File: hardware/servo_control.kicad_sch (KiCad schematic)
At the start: 4 parts, among them J5 Conn_01x03, J6 Conn_01x03, J7 Conn_01x03, J8 Conn_01x03

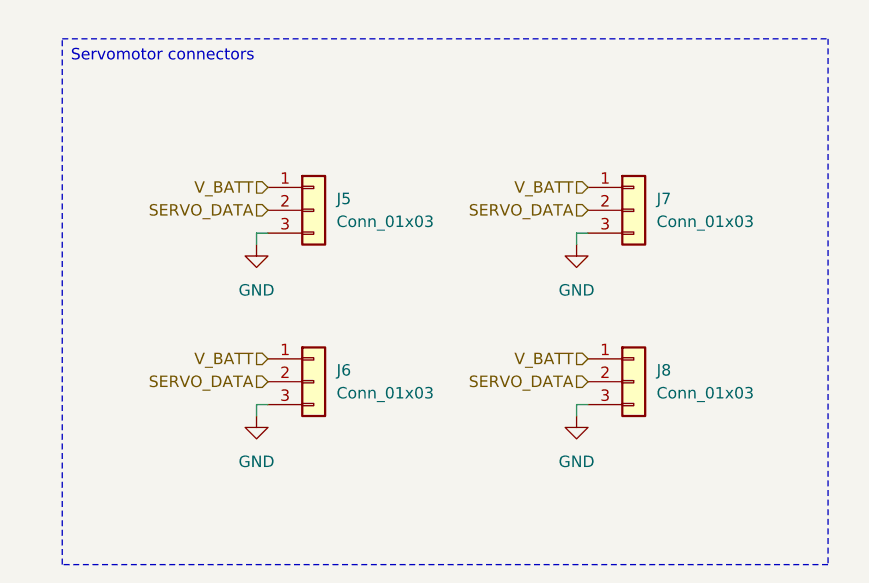
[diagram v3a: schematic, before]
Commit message: Adding test points
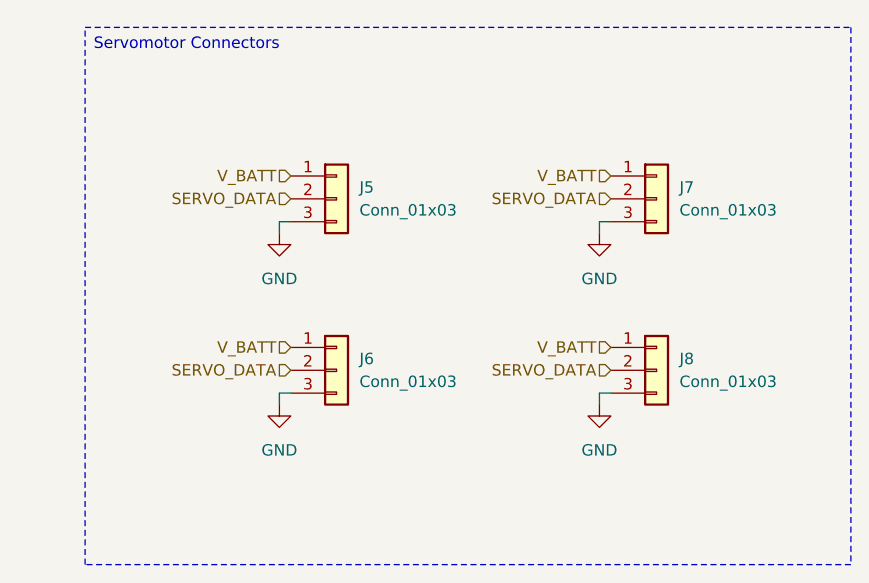
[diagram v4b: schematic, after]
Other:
- moved on the sheet: J5, J6, J7, J8
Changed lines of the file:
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@@
 		(comment 1 "Ousmane THIONGANE")
 	)
-	(text_box "Servomotor connectors"
+	(text_box "Servomotor Connectors"
 		(exclude_from_sim no)
-		(at 104.14 72.39 0)
-		(size 85.09 58.42)
+		(at 106.68 71.12 0)
+		(size 85.09 59.69)
 		(margins 0.9525 0.9525 0.9525 0.9525)
 		(stroke
@@
 	(wire
 		(pts
-			(xy 161.29 113.03) (xy 161.29 114.3)
+			(xy 163.83 111.76) (xy 163.83 113.03)
 		)
 		(stroke
@@
 	(wire
 		(pts
-			(xy 162.56 93.98) (xy 161.29 93.98)
+			(xy 165.1 92.71) (xy 163.83 92.71)
 		)
 		(stroke
@@
 	(wire
 		(pts
-			(xy 125.73 93.98) (xy 125.73 95.25)
+			(xy 128.27 92.71) (xy 128.27 93.98)
 		)
 		(stroke
@@
 	(wire
 		(pts
-			(xy 127 113.03) (xy 125.73 113.03)
+			(xy 129.54 111.76) (xy 128.27 111.76)
 		)
 		(stroke
@@
 	(wire
 		(pts
-			(xy 162.56 113.03) (xy 161.29 113.03)
+			(xy 165.1 111.76) (xy 163.83 111.76)
 		)
 		(stroke
@@
 	(wire
 		(pts
-			(xy 127 93.98) (xy 125.73 93.98)
+			(xy 129.54 92.71) (xy 128.27 92.71)
 		)
 		(stroke
@@
 	(wire
 		(pts
-			(xy 125.73 113.03) (xy 125.73 114.3)
+			(xy 128.27 111.76) (xy 128.27 113.03)
 		)
 		(stroke
@@
 	(wire
 		(pts
-			(xy 161.29 93.98) (xy 161.29 95.25)
+			(xy 163.83 92.71) (xy 163.83 93.98)
 		)
 		(stroke
@@
 	(hierarchical_label "SERVO_DATA"
 		(shape input)
-		(at 127 110.49 180)
+		(at 129.54 109.22 180)
 		(effects
 			(font
@@
 	(hierarchical_label "SERVO_DATA"
 		(shape input)
-		(at 162.56 91.44 180)
+		(at 165.1 90.17 180)
 		(effects
 			(font
@@
 	(hierarchical_label "SERVO_DATA"
 		(shape input)
-		(at 127 91.44 180)
+		(at 129.54 90.17 180)
 		(effects
 			(font
@@
 	(hierarchical_label "V_BATT"
 		(shape input)
-		(at 162.56 88.9 180)
+		(at 165.1 87.63 180)
 		(effects
 			(font
@@
 	(hierarchical_label "SERVO_DATA"
 		(shape input)
-		(at 162.56 110.49 180)
+		(at 165.1 109.22 180)
 		(effects
 			(font
@@
 	(hierarchical_label "V_BATT"
 		(shape input)
-		(at 127 107.95 180)
+		(at 129.54 106.68 180)
 		(effects
 			(font
@@
 	(hierarchical_label "V_BATT"
 		(shape input)
-		(at 127 88.9 180)
+		(at 129.54 87.63 180)
 		(effects
 			(font
@@
 	(hierarchical_label "V_BATT"
 		(shape input)
-		(at 162.56 107.95 180)
+		(at 165.1 106.68 180)
 		(effects
 			(font
@@
 	(symbol
 		(lib_id "power:GND")
-		(at 161.29 95.25 0)
+		(at 163.83 93.98 0)
 		(unit 1)
 		(exclude_from_sim no)
@@
 		(fields_autoplaced yes)
 		(property "Reference" "#PWR056"
-			(at 161.29 101.6 0)
+			(at 163.83 100.33 0)
 			(effects
 				(font
@@
 		)
 		(property "Value" "GND"
-			(at 161.29 100.33 0)
+			(at 163.83 99.06 0)
 			(effects
 				(font
@@
 		)
 		(property "Footprint" ""
-			(at 161.29 95.25 0)
+			(at 163.83 93.98 0)
 			(effects
 				(font
@@
 		)
 		(property "Datasheet" ""
-			(at 161.29 95.25 0)
+			(at 163.83 93.98 0)
 			(effects
 				(font
@@
 		)
 		(property "Description" "Power symbol creates a global label with name \"GND\" , ground"
-			(at 161.29 95.25 0)
+			(at 163.83 93.98 0)
 			(effects
 				(font
@@
 	(symbol
 		(lib_id "power:GND")
-		(at 125.73 95.25 0)
+		(at 128.27 93.98 0)
 		(unit 1)
 		(exclude_from_sim no)
@@
 		(fields_autoplaced yes)
 		(property "Reference" "#PWR054"
-			(at 125.73 101.6 0)
+			(at 128.27 100.33 0)
 			(effects
 				(font
@@
 		)
 		(property "Value" "GND"
-			(at 125.73 100.33 0)
+			(at 128.27 99.06 0)
 			(effects
 				(font
@@
 		)
 		(property "Footprint" ""
-			(at 125.73 95.25 0)
+			(at 128.27 93.98 0)
 			(effects
 				(font
@@
 		)
 		(property "Datasheet" ""
-			(at 125.73 95.25 0)
+			(at 128.27 93.98 0)
 			(effects
 				(font
@@
 		)
 		(property "Description" "Power symbol creates a global label with name \"GND\" , ground"
-			(at 125.73 95.25 0)
+			(at 128.27 93.98 0)
 			(effects
 				(font
@@
 	(symbol
 		(lib_id "Connector_Generic:Conn_01x03")
-		(at 132.08 110.49 0)
+		(at 134.62 109.22 0)
 		(unit 1)
 		(exclude_from_sim no)
@@
 		(fields_autoplaced yes)
 		(property "Reference" "J6"
-			(at 134.62 109.2199 0)
+			(at 137.16 107.9499 0)
 			(effects
 				(font
@@
 		)
 		(property "Value" "Conn_01x03"
-			(at 134.62 111.7599 0)
+			(at 137.16 110.4899 0)
 			(effects
 				(font
@@
 		)
 		(property "Footprint" ""
-			(at 132.08 110.49 0)
+			(at 134.62 109.22 0)
 			(effects
 				(font
@@
 		)
 		(property "Datasheet" "~"
-			(at 132.08 110.49 0)
+			(at 134.62 109.22 0)
 			(effects
 				(font
@@
 		)
 		(property "Description" "Generic connector, single row, 01x03, script generated (kicad-library-utils/schlib/autogen/connector/)"
-			(at 132.08 110.49 0)
+			(at 134.62 109.22 0)
 			(effects
 				(font
@@
 	(symbol
 		(lib_id "power:GND")
-		(at 161.29 114.3 0)
+		(at 163.83 113.03 0)
 		(unit 1)
 		(exclude_from_sim no)
@@
 		(fields_autoplaced yes)
 		(property "Reference" "#PWR057"
-			(at 161.29 120.65 0)
+			(at 163.83 119.38 0)
 			(effects
 				(font
@@
 		)
 		(property "Value" "GND"
-			(at 161.29 119.38 0)
+			(at 163.83 118.11 0)
 			(effects
 				(font
@@
 		)
 		(property "Footprint" ""
-			(at 161.29 114.3 0)
+			(at 163.83 113.03 0)
 			(effects
 				(font
@@
 		)
 		(property "Datasheet" ""
-			(at 161.29 114.3 0)
+			(at 163.83 113.03 0)
 			(effects
 				(font
@@
 		)
 		(property "Description" "Power symbol creates a global label with name \"GND\" , ground"
-			(at 161.29 114.3 0)
+			(at 163.83 113.03 0)
 			(effects
 				(font
@@
 	(symbol
 		(lib_id "Connector_Generic:Conn_01x03")
-		(at 167.64 110.49 0)
+		(at 170.18 109.22 0)
 		(unit 1)
 		(exclude_from_sim no)
@@
 		(fields_autoplaced yes)
 		(property "Reference" "J8"
-			(at 170.18 109.2199 0)
+			(at 172.72 107.9499 0)
 			(effects
 				(font
@@
 		)
 		(property "Value" "Conn_01x03"
-			(at 170.18 111.7599 0)
+			(at 172.72 110.4899 0)
 			(effects
 				(font
@@
 		)
 		(property "Footprint" ""
-			(at 167.64 110.49 0)
+			(at 170.18 109.22 0)
 			(effects
 				(font
@@
 		)
 		(property "Datasheet" "~"
-			(at 167.64 110.49 0)
+			(at 170.18 109.22 0)
 			(effects
 				(font
@@
 		)
 		(property "Description" "Generic connector, single row, 01x03, script generated (kicad-library-utils/schlib/autogen/connector/)"
-			(at 167.64 110.49 0)
+			(at 170.18 109.22 0)
 			(effects
 				(font
@@
 	(symbol
 		(lib_id "power:GND")
-		(at 125.73 114.3 0)
+		(at 128.27 113.03 0)
 		(unit 1)
 		(exclude_from_sim no)
@@
 		(fields_autoplaced yes)
 		(property "Reference" "#PWR055"
-			(at 125.73 120.65 0)
+			(at 128.27 119.38 0)
 			(effects
 				(font
@@
 		)
 		(property "Value" "GND"
-			(at 125.73 119.38 0)
+			(at 128.27 118.11 0)
 			(effects
 				(font
@@
 		)
 		(property "Footprint" ""
-			(at 125.73 114.3 0)
+			(at 128.27 113.03 0)
 			(effects
 				(font
@@
 		)
 		(property "Datasheet" ""
-			(at 125.73 114.3 0)
+			(at 128.27 113.03 0)
 			(effects
 				(font
@@
 		)
 		(property "Description" "Power symbol creates a global label with name \"GND\" , ground"
-			(at 125.73 114.3 0)
+			(at 128.27 113.03 0)
 			(effects
 				(font
@@
 	(symbol
 		(lib_id "Connector_Generic:Conn_01x03")
-		(at 167.64 91.44 0)
+		(at 170.18 90.17 0)
 		(unit 1)
 		(exclude_from_sim no)
@@
 		(fields_autoplaced yes)
 		(property "Reference" "J7"
-			(at 170.18 90.1699 0)
+			(at 172.72 88.8999 0)
 			(effects
 				(font
@@
 		)
 		(property "Value" "Conn_01x03"
-			(at 170.18 92.7099 0)
+			(at 172.72 91.4399 0)
 			(effects
 				(font
@@
 		)
 		(property "Footprint" ""
-			(at 167.64 91.44 0)
+			(at 170.18 90.17 0)
 			(effects
 				(font
@@
 		)
 		(property "Datasheet" "~"
-			(at 167.64 91.44 0)
+			(at 170.18 90.17 0)
 			(effects
 				(font
@@
 		)
 		(property "Description" "Generic connector, single row, 01x03, script generated (kicad-library-utils/schlib/autogen/connector/)"
-			(at 167.64 91.44 0)
+			(at 170.18 90.17 0)
 			(effects
 				(font
@@
 	(symbol
 		(lib_id "Connector_Generic:Conn_01x03")
-		(at 132.08 91.44 0)
+		(at 134.62 90.17 0)
 		(unit 1)
 		(exclude_from_sim no)
@@
 		(fields_autoplaced yes)
 		(property "Reference" "J5"
-			(at 134.62 90.1699 0)
+			(at 137.16 88.8999 0)
 			(effects
 				(font
@@
 		)
 		(property "Value" "Conn_01x03"
-			(at 134.62 92.7099 0)
+			(at 137.16 91.4399 0)
 			(effects
 				(font
@@
 		)
 		(property "Footprint" ""
-			(at 132.08 91.44 0)
+			(at 134.62 90.17 0)
 			(effects
 				(font
@@
 		)
 		(property "Datasheet" "~"
-			(at 132.08 91.44 0)
+			(at 134.62 90.17 0)
 			(effects
 				(font
@@
 		)
 		(property "Description" "Generic connector, single row, 01x03, script generated (kicad-library-utils/schlib/autogen/connector/)"
-			(at 132.08 91.44 0)
+			(at 134.62 90.17 0)
 			(effects
 				(font

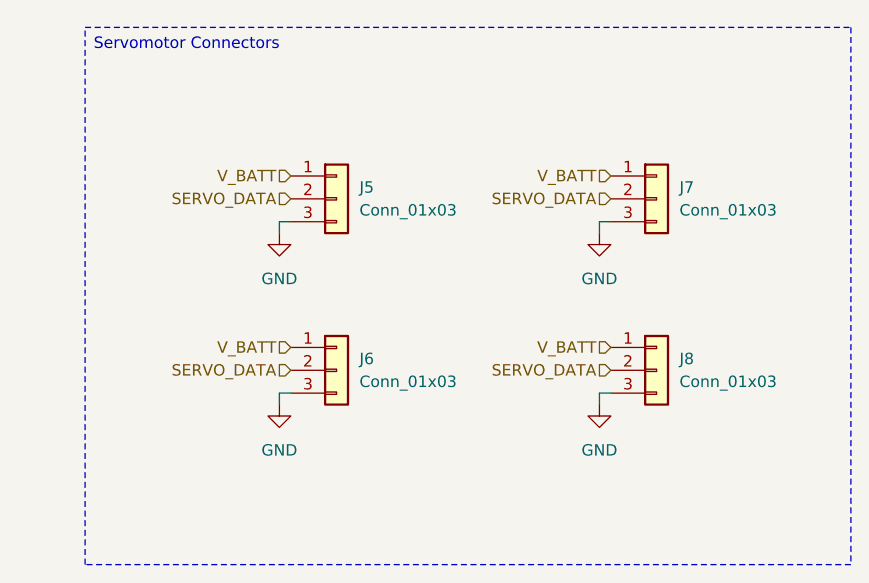
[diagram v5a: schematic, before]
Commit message: Adding footprint & symbol folders
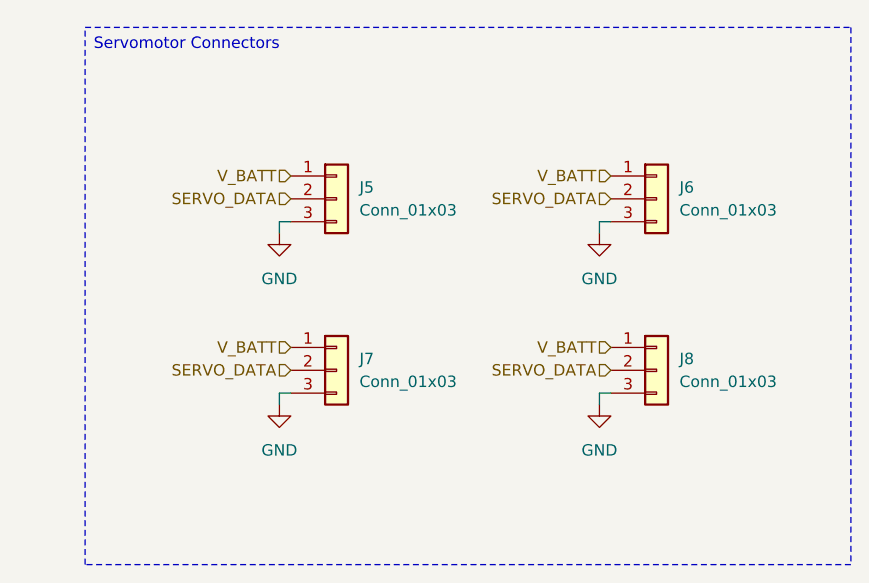
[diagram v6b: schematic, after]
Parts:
- renumbered J7 to J6, J6 to J7
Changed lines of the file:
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@@
 		(dnp no)
 		(fields_autoplaced yes)
-		(property "Reference" "#PWR061"
+		(property "Reference" "#PWR060"
 			(at 163.83 100.33 0)
 			(effects
@@
 			(project "chromapi_motherboard_v1"
 				(path "/d1a31f26-03e0-43e1-89c1-031fe31befc5/65907df6-508b-450c-8c31-d637ad608dec"
-					(reference "#PWR061")
+					(reference "#PWR060")
 					(unit 1)
 				)
@@
 		(dnp no)
 		(fields_autoplaced yes)
-		(property "Reference" "J6"
+		(property "Reference" "J7"
 			(at 137.16 107.9499 0)
 			(effects
@@
 			(project "chromapi_motherboard_v1"
 				(path "/d1a31f26-03e0-43e1-89c1-031fe31befc5/65907df6-508b-450c-8c31-d637ad608dec"
-					(reference "J6")
+					(reference "J7")
 					(unit 1)
 				)
@@
 		(dnp no)
 		(fields_autoplaced yes)
-		(property "Reference" "#PWR060"
+		(property "Reference" "#PWR061"
 			(at 128.27 119.38 0)
 			(effects
@@
 			(project "chromapi_motherboard_v1"
 				(path "/d1a31f26-03e0-43e1-89c1-031fe31befc5/65907df6-508b-450c-8c31-d637ad608dec"
-					(reference "#PWR060")
+					(reference "#PWR061")
 					(unit 1)
 				)
@@
 		(dnp no)
 		(fields_autoplaced yes)
-		(property "Reference" "J7"
+		(property "Reference" "J6"
 			(at 172.72 88.8999 0)
 			(effects
@@
 			(project "chromapi_motherboard_v1"
 				(path "/d1a31f26-03e0-43e1-89c1-031fe31befc5/65907df6-508b-450c-8c31-d637ad608dec"
-					(reference "J7")
-					(unit 1)
-				)
+					(reference "J6")
+					(unit 1)
+				)

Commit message: Adding footprints
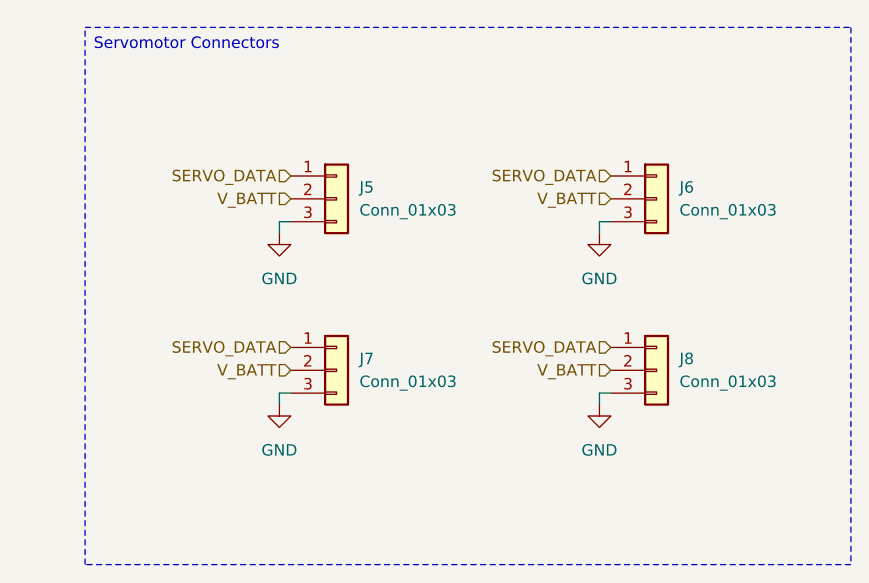
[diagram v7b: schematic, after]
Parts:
- J5, J6, J7, J8: footprint (none) -> Connector_Molex:Molex_SPOX_5267-03A_1x03_P2.50mm_Vertical
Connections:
- net SERVO_DATA: now also J5.1 (Pin_1), J6.1 (Pin_1), J7.1 (Pin_1), J8.1 (Pin_1); no longer J5.2 (Pin_2), J6.2 (Pin_2), J7.2 (Pin_2), J8.2 (Pin_2)
- net V_BATT: now also J5.2 (Pin_2), J6.2 (Pin_2), J7.2 (Pin_2), J8.2 (Pin_2); no longer J5.1 (Pin_1), J6.1 (Pin_1), J7.1 (Pin_1), J8.1 (Pin_1)
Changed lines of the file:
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@@
+		)
+	)
+	(hierarchical_label "V_BATT"
+		(shape input)
+		(at 129.54 90.17 180)
+		(effects
+			(font
+				(size 1.27 1.27)
+			)
+			(justify right)
+		)
+	)
+	(hierarchical_label "V_BATT"
+		(shape input)
+		(at 129.54 109.22 180)
+		(effects
+			(font
+				(size 1.27 1.27)
+			)
+			(justify right)
 		)
 	)
 	(hierarchical_label "SERVO_DATA"
 		(shape input)
-		(at 129.54 109.22 180)
+		(at 129.54 106.68 180)
 		(effects
 			(font
@@
 	(hierarchical_label "SERVO_DATA"
 		(shape input)
+		(at 129.54 87.63 180)
+		(effects
+			(font
+				(size 1.27 1.27)
+			)
+			(justify right)
+		)
+	)
+	(hierarchical_label "V_BATT"
+		(shape input)
+		(at 165.1 109.22 180)
+		(effects
+			(font
+				(size 1.27 1.27)
+			)
+			(justify right)
+		)
+	)
+	(hierarchical_label "V_BATT"
+		(shape input)
 		(at 165.1 90.17 180)
 		(effects
@@
 	(hierarchical_label "SERVO_DATA"
 		(shape input)
-		(at 129.54 90.17 180)
-		(effects
-			(font
-				(size 1.27 1.27)
-			)
-			(justify right)
-		)
-	)
-	(hierarchical_label "V_BATT"
-		(shape input)
 		(at 165.1 87.63 180)
 		(effects
@@
 	)
 	(hierarchical_label "SERVO_DATA"
-		(shape input)
-		(at 165.1 109.22 180)
-		(effects
-			(font
-				(size 1.27 1.27)
-			)
-			(justify right)
-		)
-	)
-	(hierarchical_label "V_BATT"
-		(shape input)
-		(at 129.54 106.68 180)
-		(effects
-			(font
-				(size 1.27 1.27)
-			)
-			(justify right)
-		)
-	)
-	(hierarchical_label "V_BATT"
-		(shape input)
-		(at 129.54 87.63 180)
-		(effects
-			(font
-				(size 1.27 1.27)
-			)
-			(justify right)
-		)
-	)
-	(hierarchical_label "V_BATT"
 		(shape input)
 		(at 165.1 106.68 180)
@@
 			)
 		)
-		(property "Footprint" ""
+		(property "Footprint" "Connector_Molex:Molex_SPOX_5267-03A_1x03_P2.50mm_Vertical"
 			(at 134.62 109.22 0)
 			(effects
@@
 			)
 		)
-		(property "Footprint" ""
+		(property "Footprint" "Connector_Molex:Molex_SPOX_5267-03A_1x03_P2.50mm_Vertical"
 			(at 170.18 109.22 0)
 			(effects
@@
 			)
 		)
-		(property "Footprint" ""
+		(property "Footprint" "Connector_Molex:Molex_SPOX_5267-03A_1x03_P2.50mm_Vertical"
 			(at 170.18 90.17 0)
 			(effects
@@
 			)
 		)
-		(property "Footprint" ""
+		(property "Footprint" "Connector_Molex:Molex_SPOX_5267-03A_1x03_P2.50mm_Vertical"
 			(at 134.62 90.17 0)
 			(effects
